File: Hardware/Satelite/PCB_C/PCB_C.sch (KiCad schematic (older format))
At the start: 38 parts, among them IC1 MCP1501T-33E_CHY, IC3 BQ24392RSER, J1 Conn_01x06, J3 Conector_PCB_B-C, J4 Conector_Expansion_CanSat, J5 USB_B_Micro, J6 Conn_02x03_Counter_Clockwise, M1 Spacer, M2 Spacer, M3 Spacer, U1 NTB0104BQ,115, U2 TCA9802DGKR, U3 ESP32-WROOM-32, U4 NTB0104BQ,115, U7 PIC16LF18325-ISL, Y1 LFXTAL016178

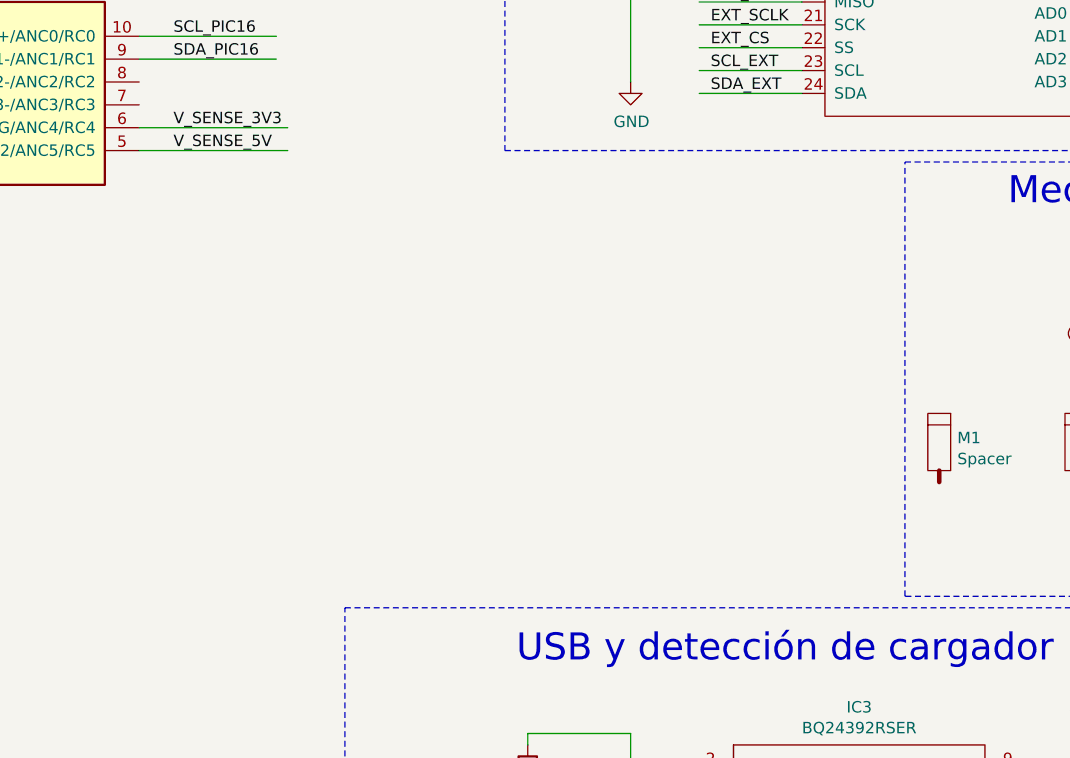
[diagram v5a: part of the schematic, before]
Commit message: Agregados testpoint a PCB_C
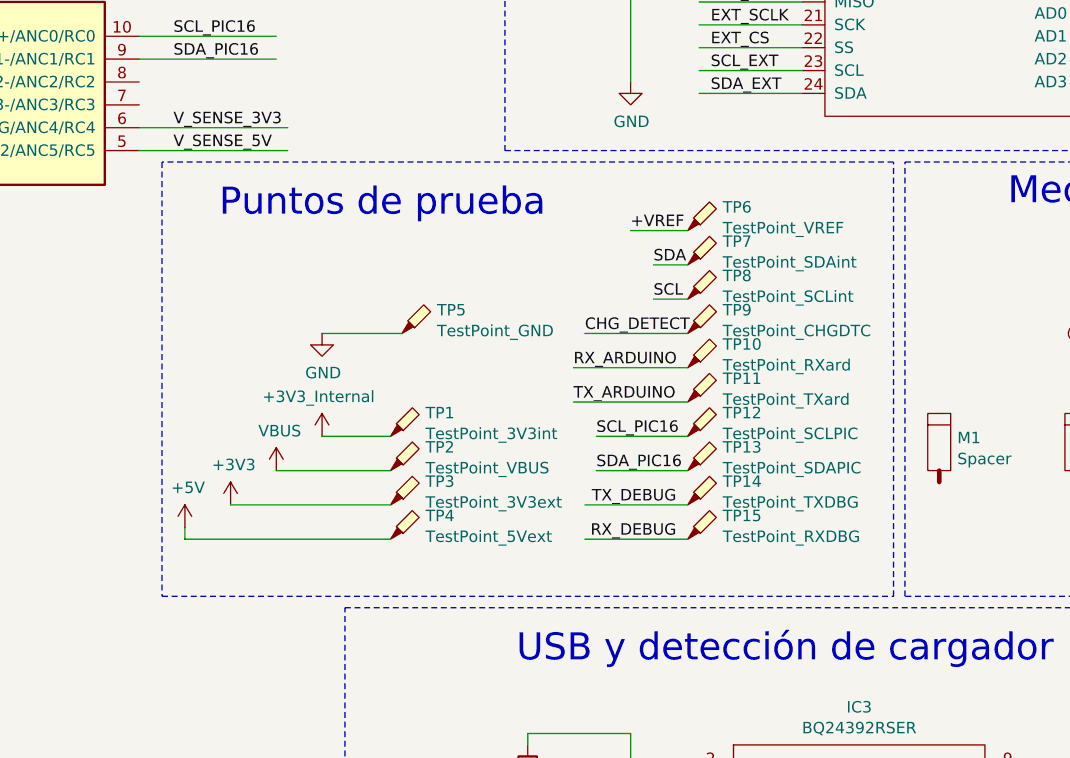
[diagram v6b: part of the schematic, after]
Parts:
- added TP1: TestPoint_3V3int, TestPoint:TestPoint_Pad_D1.0mm, symbol Connector:TestPoint_Probe
- added TP10: TestPoint_RXard, TestPoint:TestPoint_Pad_D1.0mm, symbol Connector:TestPoint_Probe
- added TP11: TestPoint_TXard, TestPoint:TestPoint_Pad_D1.0mm, symbol Connector:TestPoint_Probe
- added TP12: TestPoint_SCLPIC, TestPoint:TestPoint_Pad_D1.0mm, symbol Connector:TestPoint_Probe
- added TP13: TestPoint_SDAPIC, TestPoint:TestPoint_Pad_D1.0mm, symbol Connector:TestPoint_Probe
- added TP14: TestPoint_TXDBG, TestPoint:TestPoint_Pad_D1.0mm, symbol Connector:TestPoint_Probe
- added TP15: TestPoint_RXDBG, TestPoint:TestPoint_Pad_D1.0mm, symbol Connector:TestPoint_Probe
- added TP2: TestPoint_VBUS, TestPoint:TestPoint_Pad_D1.0mm, symbol Connector:TestPoint_Probe
- added TP3: TestPoint_3V3ext, TestPoint:TestPoint_Pad_D1.0mm, symbol Connector:TestPoint_Probe
- added TP4: TestPoint_5Vext, TestPoint:TestPoint_Pad_D1.0mm, symbol Connector:TestPoint_Probe
- added TP5: TestPoint_GND, TestPoint:TestPoint_THTPad_1.0x1.0mm_Drill0.5mm, symbol Connector:TestPoint_Probe
- added TP6: TestPoint_VREF, TestPoint:TestPoint_Pad_D1.0mm, symbol Connector:TestPoint_Probe
- added TP7: TestPoint_SDAint, TestPoint:TestPoint_Pad_D1.0mm, symbol Connector:TestPoint_Probe
- added TP8: TestPoint_SCLint, TestPoint:TestPoint_Pad_D1.0mm, symbol Connector:TestPoint_Probe
- added TP9: TestPoint_CHGDTC, TestPoint:TestPoint_Pad_D1.0mm, symbol Connector:TestPoint_Probe
- J4: footprint (none) -> AXTEC:Conector_Expansion_CanSat
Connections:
- wire segments 285 -> 301
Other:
- note added: "Puntos de prueba"

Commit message: Separación de GND analógico y digital
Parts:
- added NT1: Net-Tie_2, Jumper:SolderJumper-2_P1.3mm_Bridged2Bar_Pad1.0x1.5mm, symbol Device:Net-Tie_2
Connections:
- net labels added: GNDA
- wire segments 301 -> 305
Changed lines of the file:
@@
 Text Label 7900 2850 2    50   ~ 0
 SCL_PIC16
-$Comp
-L power:GND #PWR046
-U 1 1 5C5E258C
-P 8400 6500
-F 0 "#PWR046" H 8400 6250 50  0001 C CNN
-F 1 "GND" H 8404 6326 50  0000 C CNN
-F 2 "" H 8400 6500 50  0001 C CNN
-F 3 "" H 8400 6500 50  0001 C CNN
-	1    8400 6500
-	1    0    0    -1
-$EndComp
 Wire Wire Line
 	8400 6400 8400 6500
@@
 Wire Wire Line
 	2800 5950 2800 6050
-$Comp
-L power:GND #PWR06
-U 1 1 5BC4CEB3
-P 2800 6150
-F 0 "#PWR06" H 2800 5900 50  0001 C CNN
-F 1 "GND" H 2805 5977 50  0000 C CNN
-F 2 "" H 2800 6150 50  0001 C CNN
-F 3 "" H 2800 6150 50  0001 C CNN
-	1    2800 6150
-	-1   0    0    -1
-$EndComp
 Wire Wire Line
 	1400 6050 1400 6150
 Wire Wire Line
 	1500 6050 1400 6050
-$Comp
-L power:GND #PWR03
-U 1 1 5BC4AB0B
-P 1400 6150
-F 0 "#PWR03" H 1400 5900 50  0001 C CNN
-F 1 "GND" H 1405 5977 50  0000 C CNN
-F 2 "" H 1400 6150 50  0001 C CNN
-F 3 "" H 1400 6150 50  0001 C CNN
-	1    1400 6150
-	-1   0    0    -1
-$EndComp
 Wire Wire Line
 	1400 5850 1150 5850
@@
 Wire Wire Line
 	1150 6100 1150 6150
-$Comp
-L power:GND #PWR02
-U 1 1 5BC4278A
-P 1150 6150
-F 0 "#PWR02" H 1150 5900 50  0001 C CNN
-F 1 "GND" H 1155 5977 50  0000 C CNN
-F 2 "" H 1150 6150 50  0001 C CNN
-F 3 "" H 1150 6150 50  0001 C CNN
-	1    1150 6150
-	-1   0    0    -1
-$EndComp
 Wire Wire Line
 	1150 5900 1150 5850
@@
 Wire Wire Line
 	11700 6900 12050 6900
+$Comp
+L power:GNDA #PWR0103
+U 1 1 5C301DAD
+P 2800 6150
+F 0 "#PWR0103" H 2800 5900 50  0001 C CNN
+F 1 "GNDA" H 2804 5976 50  0000 C CNN
+F 2 "" H 2800 6150 50  0001 C CNN
+F 3 "" H 2800 6150 50  0001 C CNN
+	1    2800 6150
+	1    0    0    -1
+$EndComp
+$Comp
+L power:GNDA #PWR0104
+U 1 1 5C301F3D
+P 6550 6700
+F 0 "#PWR0104" H 6550 6450 50  0001 C CNN
+F 1 "GNDA" H 6554 6526 50  0000 C CNN
+F 2 "" H 6550 6700 50  0001 C CNN
+F 3 "" H 6550 6700 50  0001 C CNN
+	1    6550 6700
+	1    0    0    -1
+$EndComp
+$Comp
+L power:GND #PWR0105
+U 1 1 5C3020F0
+P 6150 6700
+F 0 "#PWR0105" H 6150 6450 50  0001 C CNN
+F 1 "GND" H 6154 6526 50  0000 C CNN
+F 2 "" H 6150 6700 50  0001 C CNN
+F 3 "" H 6150 6700 50  0001 C CNN
+	1    6150 6700
+	1    0    0    -1
+$EndComp
+Wire Wire Line
+	6150 6700 6150 6650
+Wire Wire Line
+	6550 6650 6550 6700
+$Comp
+L Device:Net-Tie_2 NT1
+U 1 1 5C31ED45
+P 6350 6650
+F 0 "NT1" H 6350 6829 50  0000 C CNN
+F 1 "Net-Tie_2" H 6350 6737 50  0000 C CNN
+F 2 "Jumper:SolderJumper-2_P1.3mm_Bridged2Bar_Pad1.0x1.5mm" H 6350 6650 50  0001 C CNN
+F 3 "~" H 6350 6650 50  0001 C CNN
+	1    6350 6650
+	1    0    0    -1
+$EndComp
+Wire Wire Line
+	6150 6650 6250 6650
+Wire Wire Line
+	6450 6650 6550 6650
+$Comp
+L power:GNDA #PWR0106
+U 1 1 5C375184
+P 1400 6150
+F 0 "#PWR0106" H 1400 5900 50  0001 C CNN
+F 1 "GNDA" H 1404 5976 50  0000 C CNN
+F 2 "" H 1400 6150 50  0001 C CNN
+F 3 "" H 1400 6150 50  0001 C CNN
+	1    1400 6150
+	1    0    0    -1
+$EndComp
+$Comp
+L power:GNDA #PWR0107
+U 1 1 5C375315
+P 1150 6150
+F 0 "#PWR0107" H 1150 5900 50  0001 C CNN
+F 1 "GNDA" H 1154 5976 50  0000 C CNN
+F 2 "" H 1150 6150 50  0001 C CNN
+F 3 "" H 1150 6150 50  0001 C CNN
+	1    1150 6150
+	1    0    0    -1
+$EndComp
+$Comp
+L power:GNDA #PWR0108
+U 1 1 5C3756B6
+P 8400 6500
+F 0 "#PWR0108" H 8400 6250 50  0001 C CNN
+F 1 "GNDA" H 8404 6326 50  0000 C CNN
+F 2 "" H 8400 6500 50  0001 C CNN
+F 3 "" H 8400 6500 50  0001 C CNN
+	1    8400 6500
+	1    0    0    -1
+$EndComp
 $EndSCHEMATC

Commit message: Corrección de DRC en PCB_C
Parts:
- removed NT1: Net-Tie_2, Jumper:SolderJumper-2_P1.3mm_Bridged2Bar_Pad1.0x1.5mm, symbol Device:Net-Tie_2
- added L1: Inductor, Inductor_SMD:L_0805_2012Metric_Pad1.15x1.40mm_HandSolder, symbol Device:L_Core_Iron
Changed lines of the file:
@@
 L power:GNDA #PWR0104
 U 1 1 5C301F3D
-P 6550 6700
-F 0 "#PWR0104" H 6550 6450 50  0001 C CNN
-F 1 "GNDA" H 6554 6526 50  0000 C CNN
-F 2 "" H 6550 6700 50  0001 C CNN
-F 3 "" H 6550 6700 50  0001 C CNN
-	1    6550 6700
+P 7200 7300
+F 0 "#PWR0104" H 7200 7050 50  0001 C CNN
+F 1 "GNDA" H 7204 7126 50  0000 C CNN
+F 2 "" H 7200 7300 50  0001 C CNN
+F 3 "" H 7200 7300 50  0001 C CNN
+	1    7200 7300
 	1    0    0    -1
 $EndComp
@@
 L power:GND #PWR0105
 U 1 1 5C3020F0
-P 6150 6700
-F 0 "#PWR0105" H 6150 6450 50  0001 C CNN
-F 1 "GND" H 6154 6526 50  0000 C CNN
-F 2 "" H 6150 6700 50  0001 C CNN
-F 3 "" H 6150 6700 50  0001 C CNN
-	1    6150 6700
+P 6700 7300
+F 0 "#PWR0105" H 6700 7050 50  0001 C CNN
+F 1 "GND" H 6704 7126 50  0000 C CNN
+F 2 "" H 6700 7300 50  0001 C CNN
+F 3 "" H 6700 7300 50  0001 C CNN
+	1    6700 7300
 	1    0    0    -1
 $EndComp
 Wire Wire Line
-	6150 6700 6150 6650
+	6700 7300 6700 7250
 Wire Wire Line
-	6550 6650 6550 6700
-$Comp
-L Device:Net-Tie_2 NT1
-U 1 1 5C31ED45
-P 6350 6650
-F 0 "NT1" H 6350 6829 50  0000 C CNN
-F 1 "Net-Tie_2" H 6350 6737 50  0000 C CNN
-F 2 "Jumper:SolderJumper-2_P1.3mm_Bridged2Bar_Pad1.0x1.5mm" H 6350 6650 50  0001 C CNN
-F 3 "~" H 6350 6650 50  0001 C CNN
-	1    6350 6650
-	1    0    0    -1
-$EndComp
+	7200 7250 7200 7300
 Wire Wire Line
-	6150 6650 6250 6650
+	6700 7250 6800 7250
 Wire Wire Line
-	6450 6650 6550 6650
+	7100 7250 7200 7250
 $Comp
 L power:GNDA #PWR0106
@@
 	1    0    0    -1
 $EndComp
+$Comp
+L Device:L_Core_Iron L1
+U 1 1 5C3B17F9
+P 6950 7250
+F 0 "L1" V 7177 7250 50  0000 C CNN
+F 1 "Inductor" V 7085 7250 50  0000 C CNN
+F 2 "Inductor_SMD:L_0805_2012Metric_Pad1.15x1.40mm_HandSolder" H 6950 7250 50  0001 C CNN
+F 3 "~" H 6950 7250 50  0001 C CNN
+	1    6950 7250
+	0    -1   -1   0
+$EndComp
 $EndSCHEMATC
